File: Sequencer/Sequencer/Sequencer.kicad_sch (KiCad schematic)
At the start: 41 parts, among them SW1 FORWARD, SW2 BACK, SW3 BACK, U1 40106, U2 40106, U3 4013, U4 40193

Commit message: misc sequencer
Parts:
- removed C1, C3, C7: 10nF, Capacitor_THT:C_Disc_D3.0mm_W1.6mm_P2.50mm, symbol Device:C
- removed C2, C4, C5, C6: 20nF, Capacitor_THT:C_Disc_D3.0mm_W1.6mm_P2.50mm, symbol Device:C
- removed D1, D2, D3, D4, D5, D6, D7, D8, D9: 1N914, Diode_THT:D_DO-35_SOD27_P7.62mm_Horizontal, symbol Diode:1N914
- removed R1, R12, R13, R18, R2, R9: 10K, Resistor_THT:R_Axial_DIN0204_L3.6mm_D1.6mm_P5.08mm_Horizontal, symbol Device:R
- removed R10, R11, R16, R4, R6: 220K, Resistor_THT:R_Axial_DIN0204_L3.6mm_D1.6mm_P5.08mm_Horizontal, symbol Device:R
- removed R14, R15, R7, R8: 47K, Resistor_THT:R_Axial_DIN0204_L3.6mm_D1.6mm_P5.08mm_Horizontal, symbol Device:R
- removed R17, R3, R5: 680K, Resistor_THT:R_Axial_DIN0204_L3.6mm_D1.6mm_P5.08mm_Horizontal, symbol Device:R
- removed SW1: FORWARD, symbol Switch:SW_Push
- removed SW2, SW3: BACK, symbol Switch:SW_Push
- removed U1, U2: 40106, Package_DIP:DIP-14_W7.62mm_Socket_LongPads, symbol 4xxx:40106
- removed U3: 4013, symbol 4xxx:4013
- removed U4: 40193, Package_DIP:DIP-16_W7.62mm_Socket_LongPads, symbol 4xxx_IEEE:40193
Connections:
- no-connect marks 2 -> 0
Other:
- added sheet connectors (connectors.kicad_sch)
- added sheet digital1 (digital1.kicad_sch)
- added sheet digital2 (digital2.kicad_sch)

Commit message: minor progress on sequencer
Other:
- added sheet digital3 (digital3.kicad_sch)
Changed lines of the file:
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@@
     (instances
       (project "Sequencer"
-        (path "/8a8c4421-b74b-4a68-822a-0aad66407659" (page "4"))
+        (path "/8a8c4421-b74b-4a68-822a-0aad66407659" (page "3"))
       )
     )
@@
     (instances
       (project "Sequencer"
-        (path "/8a8c4421-b74b-4a68-822a-0aad66407659" (page "2"))
+        (path "/8a8c4421-b74b-4a68-822a-0aad66407659" (page "6"))
       )
     )
@@
     (instances
       (project "Sequencer"
-        (path "/8a8c4421-b74b-4a68-822a-0aad66407659" (page "3"))
+        (path "/8a8c4421-b74b-4a68-822a-0aad66407659" (page "2"))
       )
     )
+  )
+  (sheet (at 139.7 101.6) (size 12.7 3.81) (fields_autoplaced)
+    (stroke (width 0.1524) (type solid))
+    (fill (color 0 0 0 0.0000))
+    (property "Sheetname" "digital3" (at 139.7 100.8884 0)
+      (effects (font (size 1.27 1.27)) (justify left bottom))
+    )
+    (property "Sheetfile" "digital3.kicad_sch" (at 139.7 105.9946 0)
+      (effects (font (size 1.27 1.27)) (justify left top))
+    )
+    (instances
+      (project "Sequencer"
+        (path "/8a8c4421-b74b-4a68-822a-0aad66407659" (page "5"))
+      )
+    )

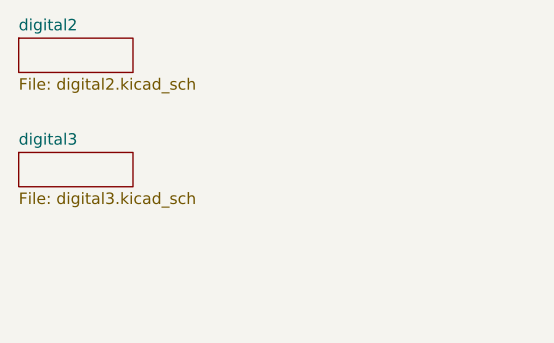
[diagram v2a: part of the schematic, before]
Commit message: Sequencer - schematic mostly complete
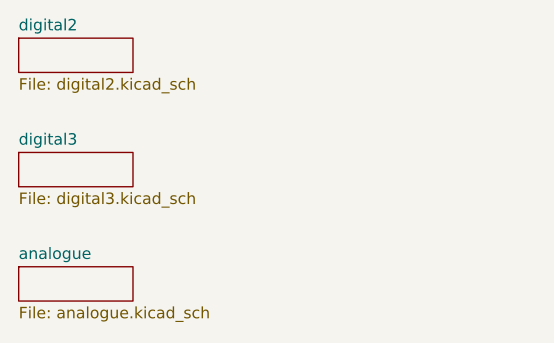
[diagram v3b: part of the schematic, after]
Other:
- added sheet analogue (analogue.kicad_sch)
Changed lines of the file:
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@@
+    )
+  )
+  (sheet (at 139.7 114.3) (size 12.7 3.81) (fields_autoplaced)
+    (stroke (width 0.1524) (type solid))
+    (fill (color 0 0 0 0.0000))
+    (property "Sheetname" "analogue" (at 139.7 113.5884 0)
+      (effects (font (size 1.27 1.27)) (justify left bottom))
+    )
+    (property "Sheetfile" "analogue.kicad_sch" (at 139.7 118.6946 0)
+      (effects (font (size 1.27 1.27)) (justify left top))
+    )
+    (instances
+      (project "Sequencer"
+        (path "/8a8c4421-b74b-4a68-822a-0aad66407659" (page "22"))
+      )
     )
   )
